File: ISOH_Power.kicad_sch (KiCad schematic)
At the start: 16 parts

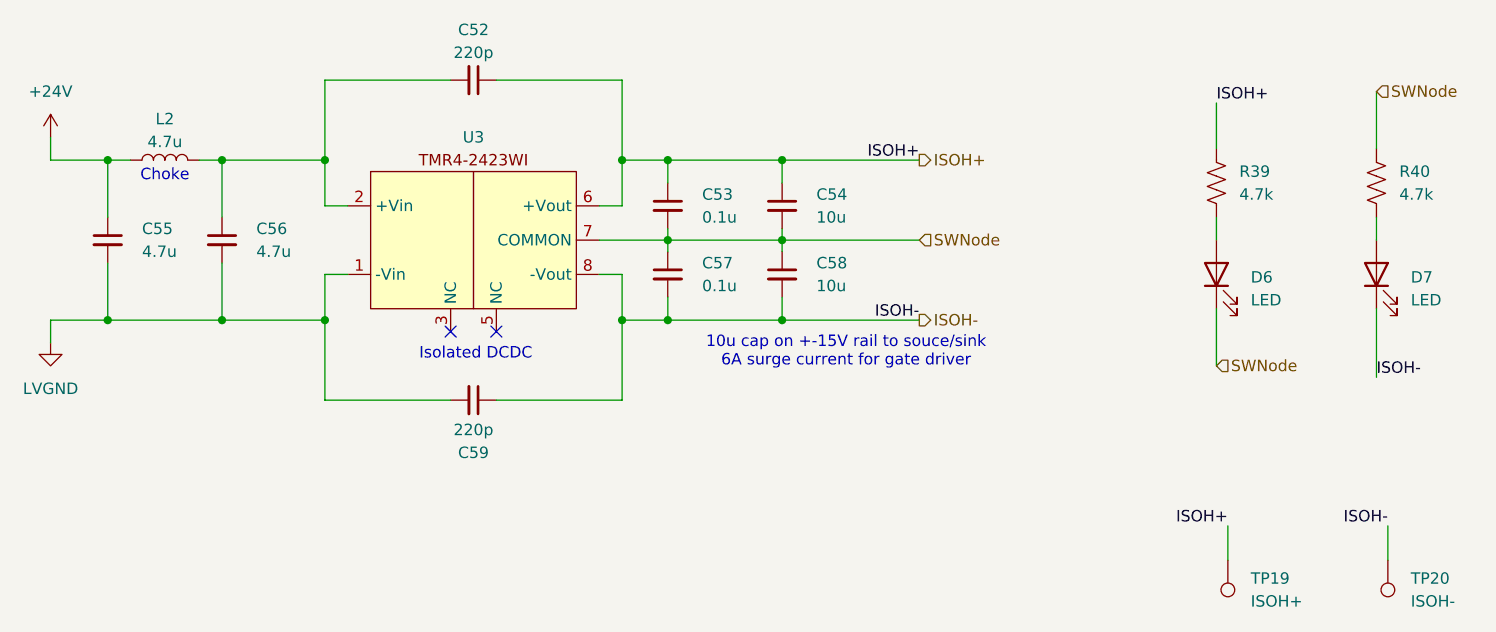
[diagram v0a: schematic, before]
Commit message: new bulk caps, new HV+,- connector placement
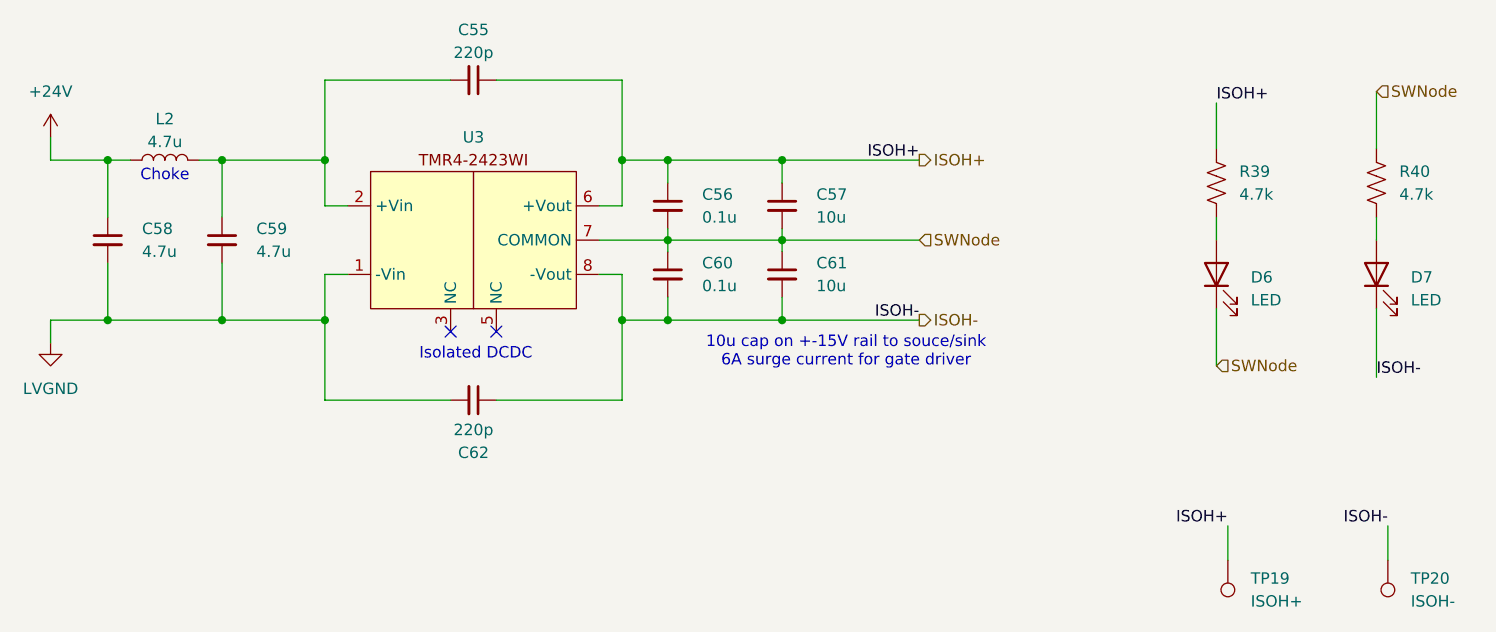
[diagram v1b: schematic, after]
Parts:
- renumbered C52 to C55, C53 to C56, C54 to C57, C55 to C58, C56 to C59, C57 to C60, C58 to C61, C59 to C62

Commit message: killed testpoints
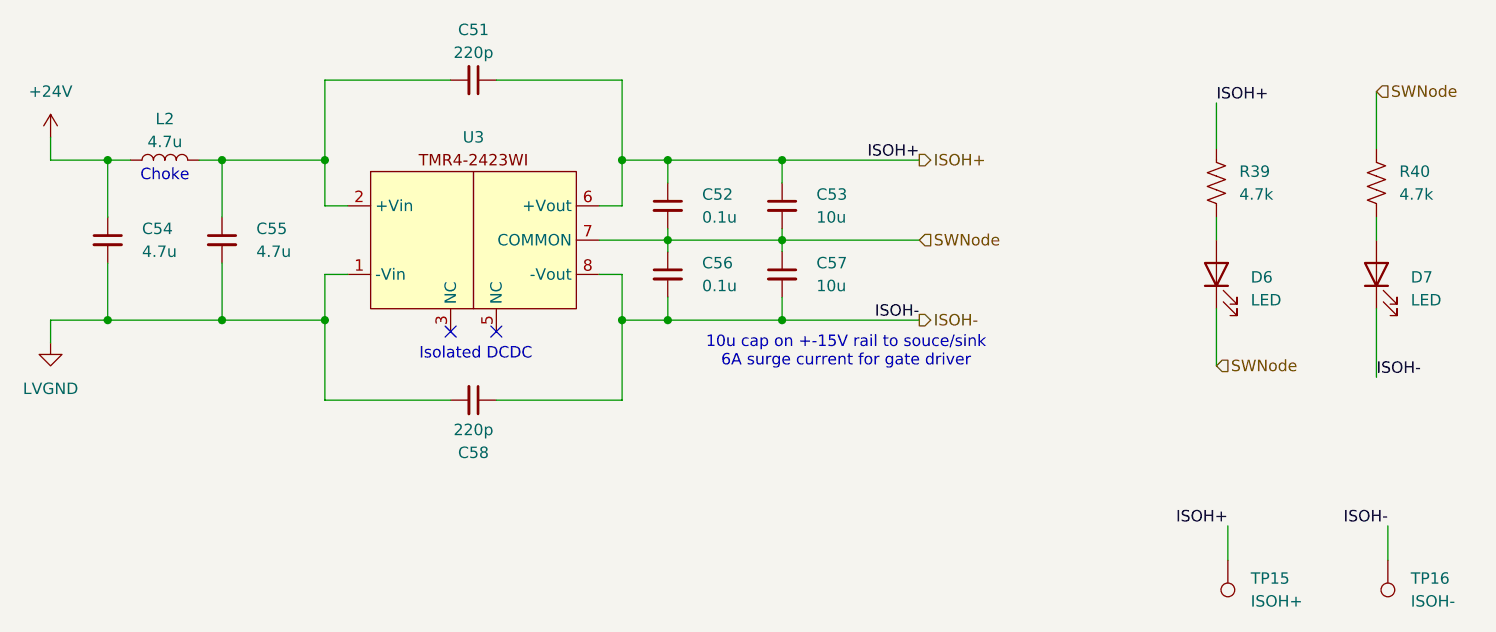
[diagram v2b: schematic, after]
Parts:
- renumbered C55 to C51, C56 to C52, C57 to C53, C58 to C54, C59 to C55, C60 to C56, C61 to C57, C62 to C58, TP19 to TP15, TP20 to TP16

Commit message: gate driver connector 1 layout and isodcdc L
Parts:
- TP15, TP16: footprint TractionInverter:KEYSTONE_5281 -> TestPoint:TestPoint_Pad_D1.5mm
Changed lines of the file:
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@@
 			)
 		)
-		(property "Footprint" "TractionInverter:KEYSTONE_5281"
+		(property "Footprint" "TestPoint:TestPoint_Pad_D1.5mm"
 			(at 222.25 128.27 0)
 			(effects
@@
 				)
 				(path "/bc91ffbf-afc6-42bb-9d28-6a3fecc21fcc/ebf1904e-ffdd-4ce1-98fa-2546468af80b/d240fb37-0ee4-4cc4-ab85-1f7fcf33acfc"
-					(reference "#PWR0200")
-					(unit 1)
-				)
-				(path "/bc91ffbf-afc6-42bb-9d28-6a3fecc21fcc/f1a23dc8-fe65-401e-b36f-fdc2d19203b3/d240fb37-0ee4-4cc4-ab85-1f7fcf33acfc"
-					(reference "#PWR0135")
+					(reference "#PWR0170")
+					(unit 1)
+				)
+				(path "/bc91ffbf-afc6-42bb-9d28-6a3fecc21fcc/f1a23dc8-fe65-401e-b36f-fdc2d19203b3/d240fb37-0ee4-4cc4-ab85-1f7fcf33acfc"
+					(reference "#PWR0115")
 					(unit 1)
 				)
@@
 			)
 		)
-		(property "Footprint" "TractionInverter:KEYSTONE_5281"
+		(property "Footprint" "TestPoint:TestPoint_Pad_D1.5mm"
 			(at 240.03 128.27 0)
 			(effects
@@
 				)
 				(path "/bc91ffbf-afc6-42bb-9d28-6a3fecc21fcc/ebf1904e-ffdd-4ce1-98fa-2546468af80b/d240fb37-0ee4-4cc4-ab85-1f7fcf33acfc"
-					(reference "#PWR0199")
-					(unit 1)
-				)
-				(path "/bc91ffbf-afc6-42bb-9d28-6a3fecc21fcc/f1a23dc8-fe65-401e-b36f-fdc2d19203b3/d240fb37-0ee4-4cc4-ab85-1f7fcf33acfc"
-					(reference "#PWR0134")
-					(unit 1)
-				)
+					(reference "#PWR0169")
+					(unit 1)
+				)
+				(path "/bc91ffbf-afc6-42bb-9d28-6a3fecc21fcc/f1a23dc8-fe65-401e-b36f-fdc2d19203b3/d240fb37-0ee4-4cc4-ab85-1f7fcf33acfc"
+					(reference "#PWR0114")
+					(unit 1)
+				)

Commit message: need to pass drc
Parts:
- renumbered TP15 to TP19, TP16 to TP20
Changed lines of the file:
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@@
 		(dnp no)
 		(fields_autoplaced yes)
-		(property "Reference" "TP15"
+		(property "Reference" "TP19"
 			(at 229.87 130.3019 0)
 			(effects
@@
 			(project "TractionInverter"
 				(path "/bc91ffbf-afc6-42bb-9d28-6a3fecc21fcc/3f7f1099-e875-4a86-860c-ef7a3936f734/d240fb37-0ee4-4cc4-ab85-1f7fcf33acfc"
-					(reference "TP15")
-					(unit 1)
-				)
-				(path "/bc91ffbf-afc6-42bb-9d28-6a3fecc21fcc/ebf1904e-ffdd-4ce1-98fa-2546468af80b/d240fb37-0ee4-4cc4-ab85-1f7fcf33acfc"
-					(reference "TP46")
-					(unit 1)
-				)
-				(path "/bc91ffbf-afc6-42bb-9d28-6a3fecc21fcc/f1a23dc8-fe65-401e-b36f-fdc2d19203b3/d240fb37-0ee4-4cc4-ab85-1f7fcf33acfc"
-					(reference "TP31")
+					(reference "TP19")
+					(unit 1)
+				)
+				(path "/bc91ffbf-afc6-42bb-9d28-6a3fecc21fcc/ebf1904e-ffdd-4ce1-98fa-2546468af80b/d240fb37-0ee4-4cc4-ab85-1f7fcf33acfc"
+					(reference "TP50")
+					(unit 1)
+				)
+				(path "/bc91ffbf-afc6-42bb-9d28-6a3fecc21fcc/f1a23dc8-fe65-401e-b36f-fdc2d19203b3/d240fb37-0ee4-4cc4-ab85-1f7fcf33acfc"
+					(reference "TP35")
 					(unit 1)
 				)
@@
 		(dnp no)
 		(fields_autoplaced yes)
-		(property "Reference" "TP16"
+		(property "Reference" "TP20"
 			(at 247.65 130.3019 0)
 			(effects
@@
 			(project "TractionInverter"
 				(path "/bc91ffbf-afc6-42bb-9d28-6a3fecc21fcc/3f7f1099-e875-4a86-860c-ef7a3936f734/d240fb37-0ee4-4cc4-ab85-1f7fcf33acfc"
-					(reference "TP16")
-					(unit 1)
-				)
-				(path "/bc91ffbf-afc6-42bb-9d28-6a3fecc21fcc/ebf1904e-ffdd-4ce1-98fa-2546468af80b/d240fb37-0ee4-4cc4-ab85-1f7fcf33acfc"
-					(reference "TP47")
-					(unit 1)
-				)
-				(path "/bc91ffbf-afc6-42bb-9d28-6a3fecc21fcc/f1a23dc8-fe65-401e-b36f-fdc2d19203b3/d240fb37-0ee4-4cc4-ab85-1f7fcf33acfc"
-					(reference "TP32")
-					(unit 1)
-				)
+					(reference "TP20")
+					(unit 1)
+				)
+				(path "/bc91ffbf-afc6-42bb-9d28-6a3fecc21fcc/ebf1904e-ffdd-4ce1-98fa-2546468af80b/d240fb37-0ee4-4cc4-ab85-1f7fcf33acfc"
+					(reference "TP51")
+					(unit 1)
+				)
+				(path "/bc91ffbf-afc6-42bb-9d28-6a3fecc21fcc/f1a23dc8-fe65-401e-b36f-fdc2d19203b3/d240fb37-0ee4-4cc4-ab85-1f7fcf33acfc"
+					(reference "TP36")
+					(unit 1)
+				)
